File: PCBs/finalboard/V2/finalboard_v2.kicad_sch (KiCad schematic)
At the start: 45 parts, among them J1 Conn_01x02_Socket, J10 Conn_01x01, J11 Conn_01x01, J12 Conn_01x01, J13 Conn_01x02_Socket, J2 Conn_01x02_Socket, J3 Conn_01x02_Socket, J4 Conn_01x02_Socket, J5 Conn_01x02_Socket, J6 USB_Conn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

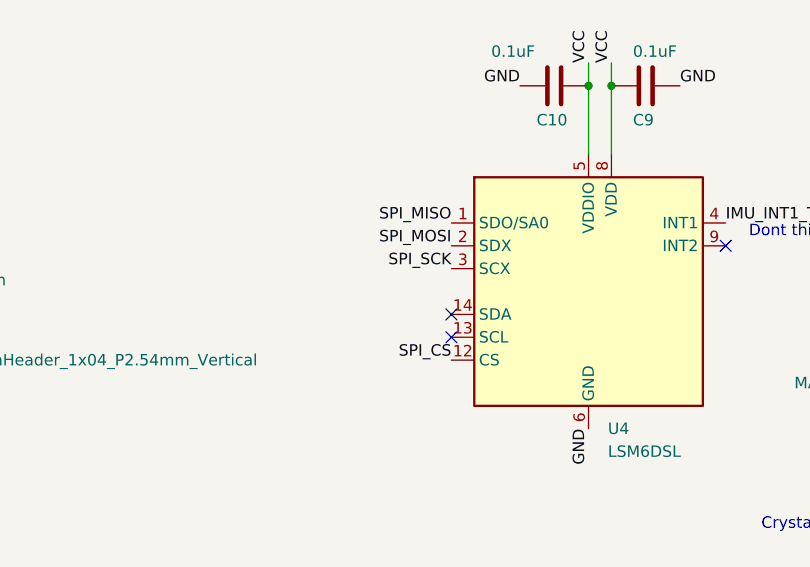
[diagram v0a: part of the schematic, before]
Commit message: Edit finalboard v2 to fix pinout on imu
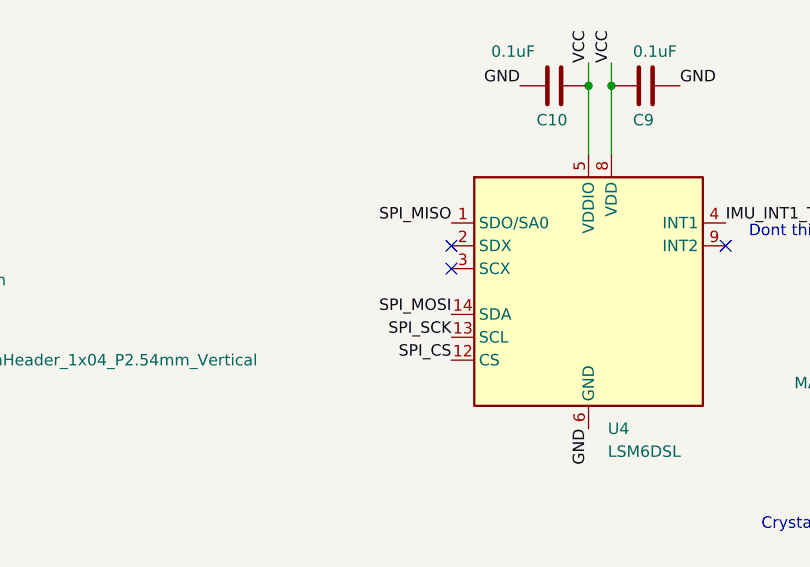
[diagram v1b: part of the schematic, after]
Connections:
- net SPI_MOSI: now also U4.14 (SDA); no longer U4.2 (SDX)
- net SPI_SCK: now also U4.13 (SCL); no longer U4.3 (SCX)
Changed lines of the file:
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@@
-	)
-	(no_connect
-		(at 127 74.93)
 	)
 	(no_connect
@@
 	)
 	(no_connect
-		(at 127 77.47)
+		(at 127 67.31)
 	)
 	(no_connect
@@
 	(no_connect
 		(at 207.01 72.39)
+	)
+	(no_connect
+		(at 127 69.85)
 	)
 	(wire
@@
 		)
 	)
+	(label "SPI_SCK"
+		(at 127 77.47 180)
+		(effects
+			(font
+				(size 1.27 1.27)
+			)
+			(justify right bottom)
+		)
+	)
 	(label "VCC"
 		(at 187.96 27.94 90)
@@
 		)
 	)
-	(label "SPI_MOSI"
-		(at 127 67.31 180)
-		(effects
-			(font
-				(size 1.27 1.27)
-			)
-			(justify right bottom)
-		)
-	)
 	(label "FSR_2+"
 		(at 74.93 142.24 270)
@@
 		)
 	)
-	(label "SPI_SCK"
-		(at 127 69.85 180)
-		(effects
-			(font
-				(size 1.27 1.27)
-			)
-			(justify right bottom)
-		)
-	)
 	(label "ADC_FSR3"
 		(at 207.01 64.77 180)
@@
 		)
 	)
+	(label "SPI_MOSI"
+		(at 127 74.93 180)
+		(effects
+			(font
+				(size 1.27 1.27)
+			)
+			(justify right bottom)
+		)
+	)
